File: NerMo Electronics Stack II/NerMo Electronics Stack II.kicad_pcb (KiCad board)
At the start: 2 copper layers, 50.5 x 21 mm, 36 parts, among them J1 PWM 5, J10 PWM 8, J11 PWM 9, J12 PWM 10, J13 PWM 11, J14 PWM 12, J15 PWM 13, J16 PWM 14, J17 PWM 15, J18 PWM 16, J2 Conn_02x06_Odd_Even, J3 PWM 1, J5 PWM 2, J6 PWM 3, J7 PWM 4, J8 PWM 6, J9 PWM 7, U5 PCA9685PW

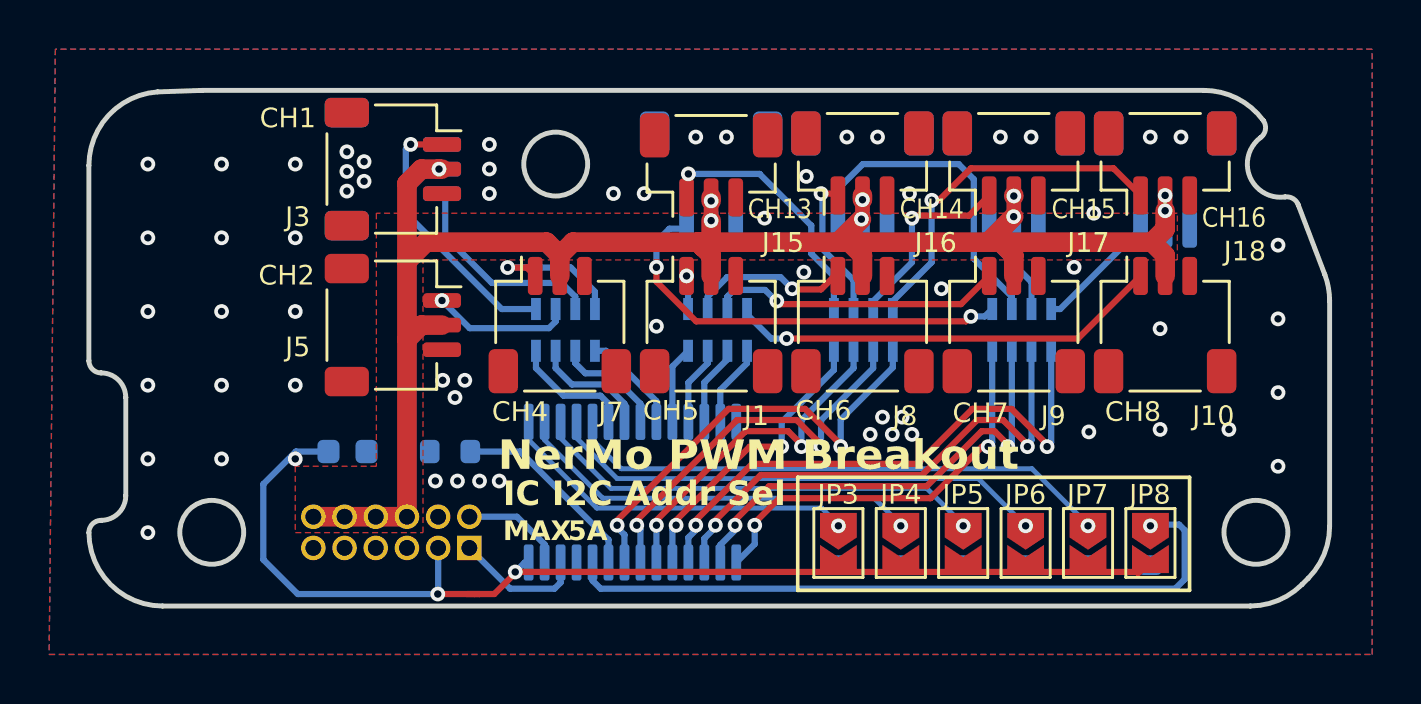
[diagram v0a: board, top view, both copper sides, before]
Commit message: fix: fixed breakout interconnect pinout
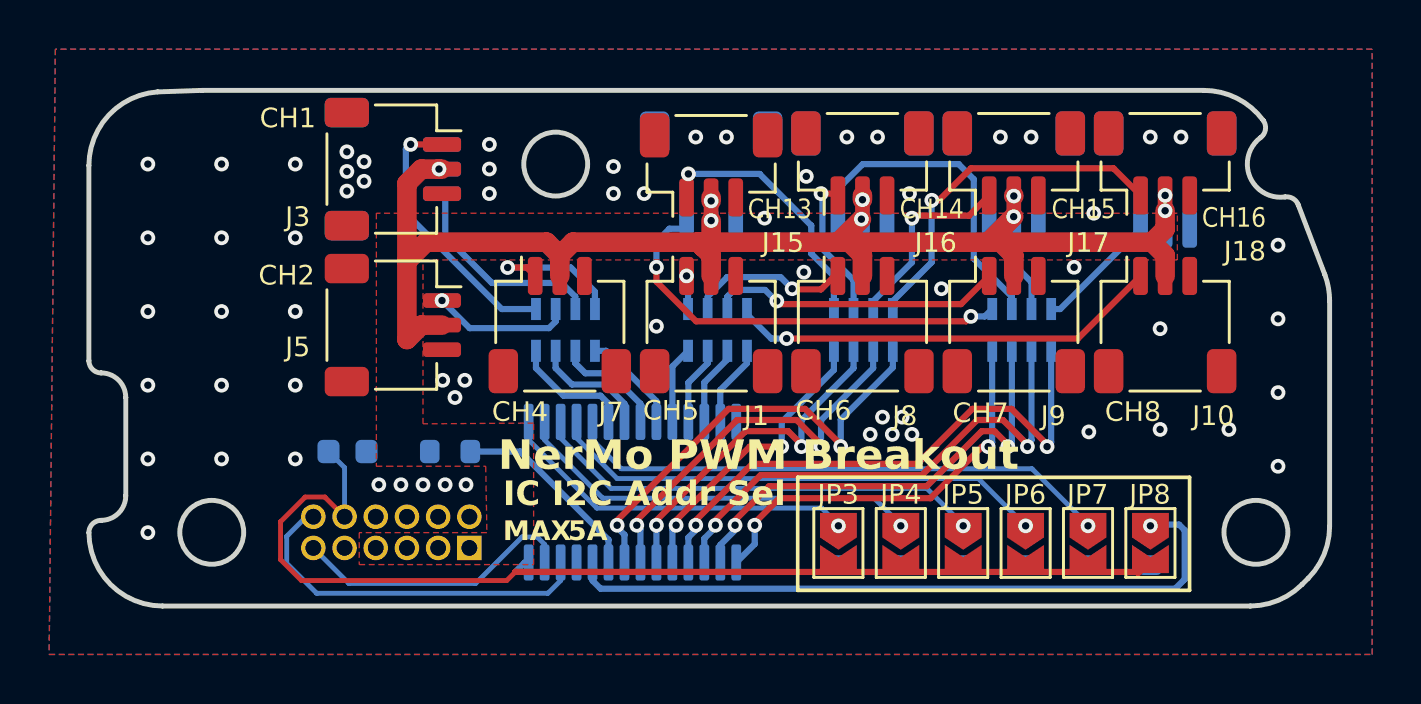
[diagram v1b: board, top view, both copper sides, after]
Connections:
- J2 pad 1: /SCL -> +6V
- J2 pad 10: +6V -> +3V3
- J2 pad 11: GND -> /SDA
- J2 pad 12: +6V -> /SCL
- J2 pad 2: /SDA -> GND
- J2 pad 3: +3V3 -> +6V
- J2 pad 5: GND -> +6V
- J2 pad 6: +6V -> GND
- J2 pad 7: GND -> +6V
- J2 pad 8: +6V -> GND
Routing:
- net +6V: track 68.0 -> 56.9 mm
- net /SCL: track 5.32 -> 15.1 mm
- net /SDA: track 4.27 -> 11.7 mm
- net +3V3: track 47.4 -> 45.4 mm, vias 2 -> 0
- net GND: vias 62 -> 64

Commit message: feat: V0.2
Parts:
- added ?: , , F.Cu at (128.5, 103.4)
- added ?: , , F.Cu at (86.0, 103.5)
- added ?: , , F.Cu at (100.1, 79.8)
- added C1: 470 µF, Capacitor_Tantalum_SMD:CP_EIA-7360-38_Kemet-E_HandSolder, B.Cu at (126.7, 96.5)
- moved C4 0.52 mm to (92.0, 100.2)
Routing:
- net +6V: vias 9 -> 12
- net GND: vias 64 -> 48
- added copper zone on B.Cu, net +6V
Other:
- board text added: "+"
- board text added: "-"
- board text added: "6V"
- board text added: "@space.zhang"
- board text added: "CH3"
- board text added: "EXT CAP"
- board text added: "NOM"
- board text added: "PCA9685"
- board text added: "Ver 0.2"
